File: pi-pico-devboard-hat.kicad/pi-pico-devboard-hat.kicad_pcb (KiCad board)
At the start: 2 copper layers, 65 x 56 mm, 28 parts, among them J1 Conn_01x24_Male, J2 I2C, J3 SDA_UP, J4 SCL_UP, J5 Conn_SPI, J6 Conn_Ext, J7 Conn_BTN, J8 Conn_LED, J9 Conn_02x03_Odd_Even, P1 Conn_02x20_Odd_Even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

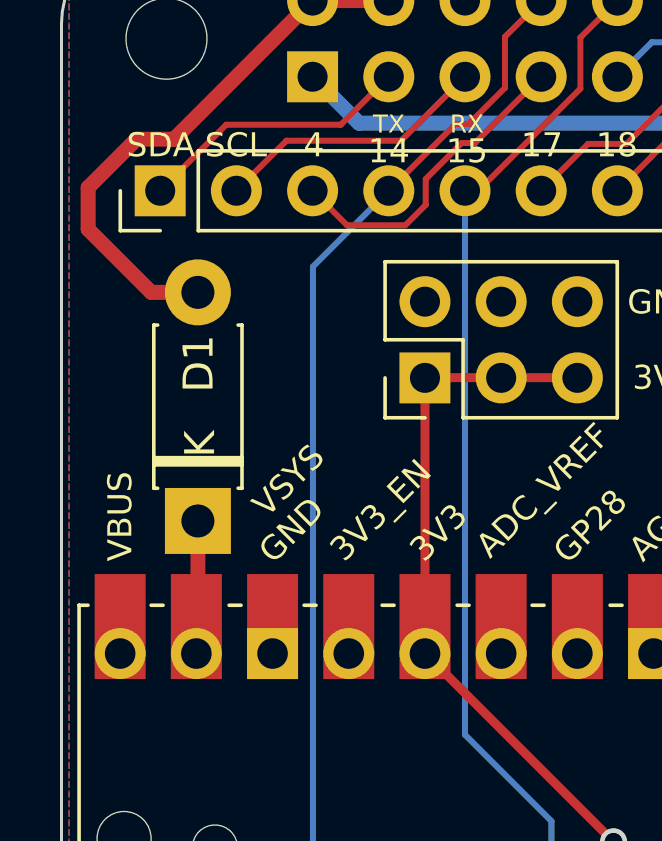
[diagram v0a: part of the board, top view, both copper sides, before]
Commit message: Rev 9: added master power-jumper
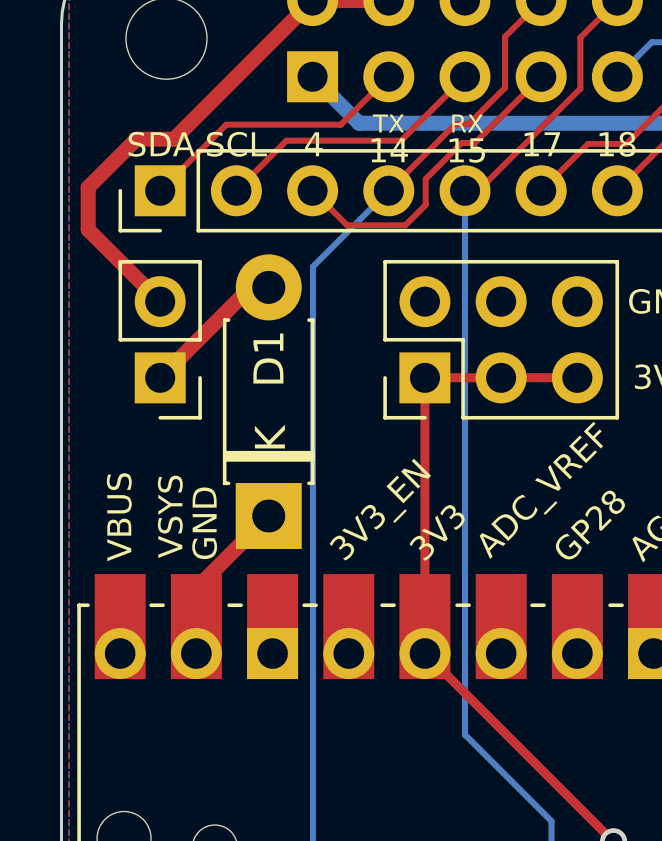
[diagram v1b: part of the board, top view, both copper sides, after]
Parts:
- added J10: Conn_Master_On, Connector_PinHeader_2.54mm:PinHeader_1x02_P2.54mm_Vertical, F.Cu at (203.3, 108.8)
- moved D1 2.37 mm to (206.9, 113.4)
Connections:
- D1 pad 2: +5V -> Net-(D1-Pad2)
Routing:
- net Net-(D1-Pad2): track 0.00 -> 5.47 mm
- net +5V: track 18.6 -> 17.4 mm
- net /VSYS: track 4.44 -> 5.66 mm
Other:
- board text added: "Rev: 9"
- board text removed: "Rev: 8"

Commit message: Rev 9.1: changed trace for 3V3
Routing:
- net /3V3: track 100.3 -> 117.6 mm, vias 1 -> 0
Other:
- net class 3V3: trace_width 0.3 -> 0.5
- board text added: "Rev: 9.1"
- board text removed: "Rev: 9"
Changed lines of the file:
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@@
   (net_class 3V3 ""
     (clearance 0.2)
-    (trace_width 0.3)
+    (trace_width 0.5)
     (via_dia 0.9)
     (via_drill 0.6)
@@
     (effects (font (size 0.8 0.8) (thickness 0.15)))
   )
-  (gr_text "Rev: 9" (at 203.9243 120.7138) (layer B.SilkS)
+  (gr_text "Rev: 9.1" (at 204.7371 120.6249) (layer B.SilkS)
     (effects (font (size 1 1) (thickness 0.15)) (justify mirror))
   )
@@
   (segment (start 204.4958 115.8243) (end 204.4958 117.996) (width 0.5) (layer F.Cu) (net 32))
   (segment (start 206.9088 113.4113) (end 204.4958 115.8243) (width 0.5) (layer F.Cu) (net 32))
-  (via (at 218.4023 124.2698) (size 0.9) (drill 0.6) (layers F.Cu B.Cu) (net 35))
-  (segment (start 212.1285 117.996) (end 218.4023 124.2698) (width 0.3) (layer F.Cu) (net 35))
   (segment (start 212.1158 117.996) (end 212.1285 117.996) (width 0.3) (layer F.Cu) (net 35))
-  (segment (start 254.5077 149.0602) (end 255.7149 147.853) (width 0.3) (layer B.Cu) (net 35))
-  (segment (start 254.1775 149.3904) (end 254.5077 149.0602) (width 0.3) (layer B.Cu) (net 35))
-  (segment (start 209.5758 147.662549) (end 209.5758 146.6726) (width 0.3) (layer B.Cu) (net 35))
-  (segment (start 211.31625 149.402999) (end 209.5758 147.662549) (width 0.3) (layer B.Cu) (net 35))
-  (segment (start 216.472001 149.402999) (end 211.31625 149.402999) (width 0.3) (layer B.Cu) (net 35))
-  (segment (start 218.4023 147.4727) (end 216.472001 149.402999) (width 0.3) (layer B.Cu) (net 35))
-  (segment (start 218.4023 124.2698) (end 218.4023 147.4727) (width 0.3) (layer B.Cu) (net 35))
-  (segment (start 224.0538 147.3457) (end 224.0538 146.6726) (width 0.3) (layer B.Cu) (net 35))
-  (segment (start 221.996501 149.402999) (end 224.0538 147.3457) (width 0.3) (layer B.Cu) (net 35))
-  (segment (start 219.558599 149.402999) (end 221.996501 149.402999) (width 0.3) (layer B.Cu) (net 35))
-  (segment (start 218.0086 147.853) (end 219.558599 149.402999) (width 0.3) (layer B.Cu) (net 35))
-  (segment (start 226.111099 149.402999) (end 224.0538 147.3457) (width 0.3) (layer B.Cu) (net 35))
-  (segment (start 230.885801 149.402999) (end 232.4358 147.853) (width 0.3) (layer B.Cu) (net 35))
-  (segment (start 226.111099 149.402999) (end 230.885801 149.402999) (width 0.3) (layer B.Cu) (net 35))
-  (segment (start 233.9732 149.3904) (end 254.1775 149.3904) (width 0.3) (layer B.Cu) (net 35))
-  (segment (start 232.4358 147.853) (end 233.9732 149.3904) (width 0.3) (layer B.Cu) (net 35))
-  (segment (start 212.1158 117.996) (end 212.1158 108.8012) (width 0.3) (layer F.Cu) (net 35))
-  (segment (start 212.1158 108.8012) (end 214.6558 108.8012) (width 0.3) (layer F.Cu) (net 35))
-  (segment (start 214.6558 108.8012) (end 217.1958 108.8012) (width 0.3) (layer F.Cu) (net 35))
+  (segment (start 207.3406 146.6726) (end 209.5758 146.6726) (width 0.5) (layer F.Cu) (net 35))
+  (segment (start 200.5461 139.8781) (end 207.3406 146.6726) (width 0.5) (layer F.Cu) (net 35))
+  (segment (start 200.5461 115.095698) (end 200.5461 139.8781) (width 0.5) (layer F.Cu) (net 35))
+  (segment (start 206.835398 108.8064) (end 200.5461 115.095698) (width 0.5) (layer F.Cu) (net 35))
+  (segment (start 212.1158 108.8064) (end 206.835398 108.8064) (width 0.5) (layer F.Cu) (net 35))
+  (segment (start 212.1158 117.996) (end 212.1158 108.8064) (width 0.5) (layer F.Cu) (net 35))
+  (segment (start 212.1158 108.8064) (end 214.6558 108.8064) (width 0.5) (layer F.Cu) (net 35))
+  (segment (start 214.6558 108.8064) (end 217.1958 108.8064) (width 0.5) (layer F.Cu) (net 35))
+  (segment (start 216.708599 149.153001) (end 218.0086 147.853) (width 0.5) (layer F.Cu) (net 35))
+  (segment (start 211.066252 149.153001) (end 216.708599 149.153001) (width 0.5) (layer F.Cu) (net 35))
+  (segment (start 209.5758 147.662549) (end 211.066252 149.153001) (width 0.5) (layer F.Cu) (net 35))
+  (segment (start 209.5758 146.6726) (end 209.5758 147.662549) (width 0.5) (layer F.Cu) (net 35))
+  (segment (start 221.573399 149.153001) (end 224.0538 146.6726) (width 0.5) (layer F.Cu) (net 35))
+  (segment (start 219.308601 149.153001) (end 221.573399 149.153001) (width 0.5) (layer F.Cu) (net 35))
+  (segment (start 218.0086 147.853) (end 219.308601 149.153001) (width 0.5) (layer F.Cu) (net 35))
+  (segment (start 231.135799 149.153001) (end 232.4358 147.853) (width 0.5) (layer F.Cu) (net 35))
+  (segment (start 226.534201 149.153001) (end 231.135799 149.153001) (width 0.5) (layer F.Cu) (net 35))
+  (segment (start 224.0538 146.6726) (end 226.534201 149.153001) (width 0.5) (layer F.Cu) (net 35))
+  (segment (start 254.414899 149.153001) (end 255.7149 147.853) (width 0.5) (layer F.Cu) (net 35))
+  (segment (start 233.735801 149.153001) (end 254.414899 149.153001) (width 0.5) (layer F.Cu) (net 35))
+  (segment (start 232.4358 147.853) (end 233.735801 149.153001) (width 0.5) (layer F.Cu) (net 35))
   (segment (start 227.3558 112.8374) (end 227.3304 112.812) (width 0.2) (layer F.Cu) (net 38))
   (segment (start 227.3558 117.996) (end 227.3558 112.8374) (width 0.2) (layer F.Cu) (net 38))

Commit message: Rev 10: reorg of I2C-pullup connector
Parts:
- removed J4: SCL_UP, Connector_PinHeader_2.54mm:PinHeader_1x02_P2.54mm_Vertical
- J3: value SDA_UP -> Conn_PU; footprint Connector_PinHeader_2.54mm:PinHeader_1x02_P2.54mm_Vertical -> Connector_PinHeader_2.54mm:PinHeader_1x04_P2.54mm_Vertical
- moved J3 8.01 mm to (212.9, 141.6), turned to 90 degrees
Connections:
- J3 pad 1: /SCL_GP3 -> Net-(J3-Pad1)
- J3 pad 2: Net-(J3-Pad2) -> /SDA_GP2
- R1 pad 2: Net-(J3-Pad2) -> Net-(J3-Pad4)
- R2 pad 2: Net-(J4-Pad2) -> Net-(J3-Pad1)
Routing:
- net Net-(J3-Pad4): track 0.00 -> 3.53 mm
- net Net-(J3-Pad2): track 3.53 -> 0.00 mm
- net Net-(J4-Pad2): track 3.35 -> 0.00 mm
- net Net-(J3-Pad1): track 0.00 -> 3.35 mm
- net /SCL_GP3: track 19.4 -> 16.5 mm
- net /SDA_GP2: track 13.8 -> 16.5 mm
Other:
- board text added: "GP2 SDA"
- board text added: "GP3 SCL"
- board text added: "Rev: 10"
- board text removed: "+"
- board text removed: "-"
- board text removed: "Rev: 9.1"
- board text removed: "SCL/GP3"
- board text removed: "SDA/GP2"

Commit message: Rev 11: connect Pi-pins GPIO16/GPIO26 to pin-connector (remove GPIO24/GPIO25 used for SWD)
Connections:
- J1 pad 11: /GPIO24(GEN5) -> /GPIO10(SPI0_MOSI)
- J1 pad 12: /GPIO25(GEN6) -> /GPIO9(SPI0_MISO)
- J1 pad 13: /GPIO10(SPI0_MOSI) -> /GPIO11(SPI0_SCK)
- J1 pad 14: /GPIO9(SPI0_MISO) -> /GPIO8(SPI0_CE_0)
- J1 pad 15: /GPIO11(SPI0_SCK) -> /GPIO7(SPI0_CE_1)
- J1 pad 16: /GPIO8(SPI0_CE_0) -> /GPIO5
- J1 pad 17: /GPIO7(SPI0_CE_1) -> /GPIO6
- J1 pad 18: /GPIO5 -> /GPIO12(PWM0)
- J1 pad 19: /GPIO6 -> /GPIO13(PWM1)
- J1 pad 20: /GPIO12(PWM0) -> /GPIO19(SPI1_MISO)
- J1 pad 21: /GPIO13(PWM1) -> /GPIO16
- J1 pad 22: /GPIO19(SPI1_MISO) -> /GPIO26
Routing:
- net /GPIO16: track 0.00 -> 7.39 mm
- net /GPIO26: track 0.00 -> 4.85 mm
- net /GPIO13(PWM1): track 6.65 -> 3.80 mm
- net /GPIO19(SPI1_MISO): track 6.65 -> 3.80 mm
- net /GPIO8(SPI0_CE_0): track 9.44 -> 7.40 mm
- net /GPIO7(SPI0_CE_1): track 8.70 -> 7.29 mm
- net /GPIO12(PWM0): track 8.83 -> 7.49 mm
- net /GPIO24(GEN5): track 39.7 -> 40.9 mm
- net /GPIO25(GEN6): track 42.0 -> 40.9 mm
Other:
- board text added: "Rev: 11"
- board text removed: "Rev: 10"

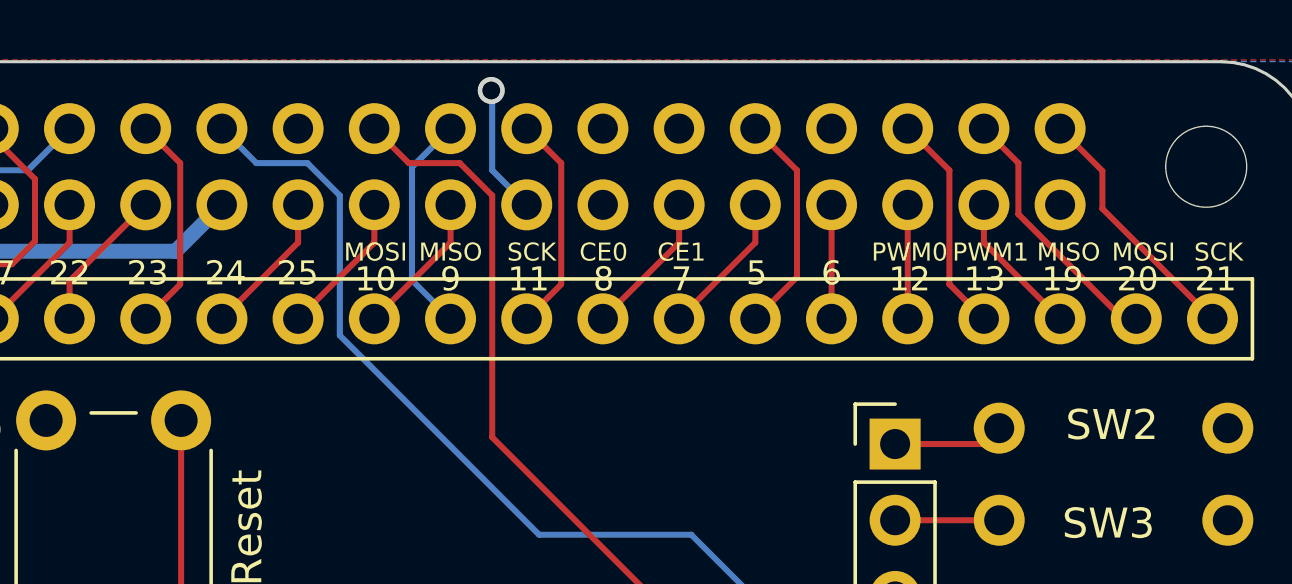
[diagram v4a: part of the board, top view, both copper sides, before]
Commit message: fixed labels of Pi-pin-connector
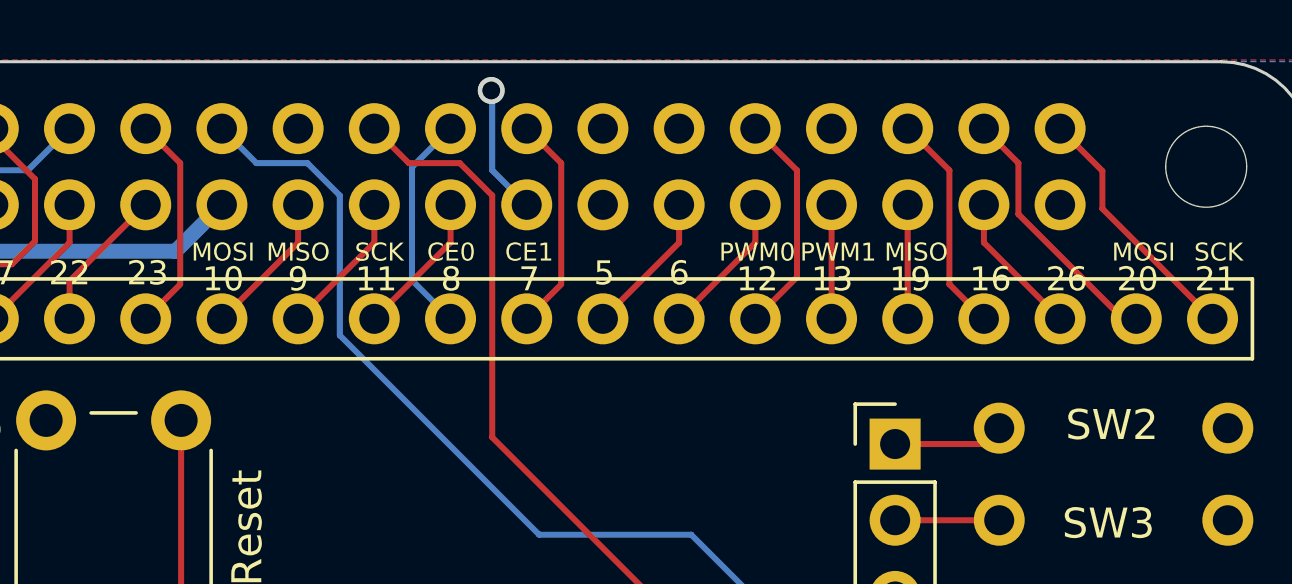
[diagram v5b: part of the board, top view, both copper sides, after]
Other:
- board text added: "16"
- board text added: "26"
- board text removed: "24"
- board text removed: "25"

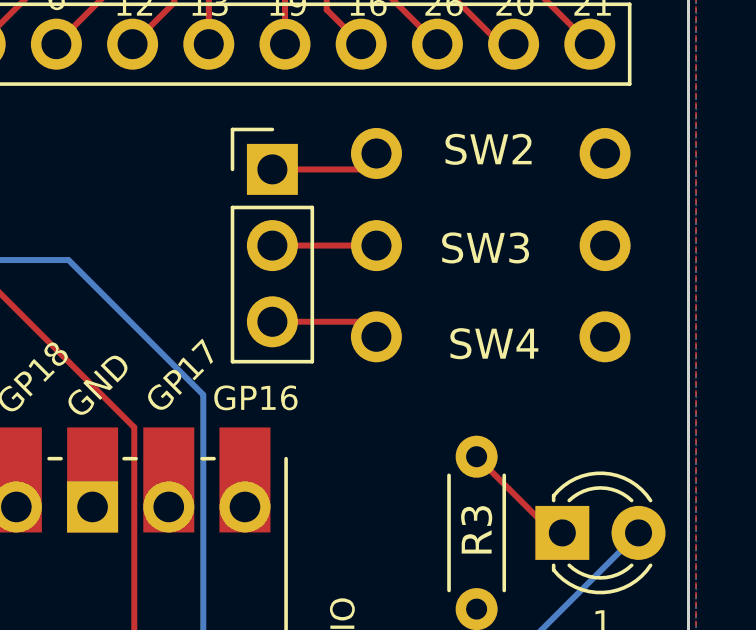
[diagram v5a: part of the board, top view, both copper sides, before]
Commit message: fixed footprint and position of SW2-SW4
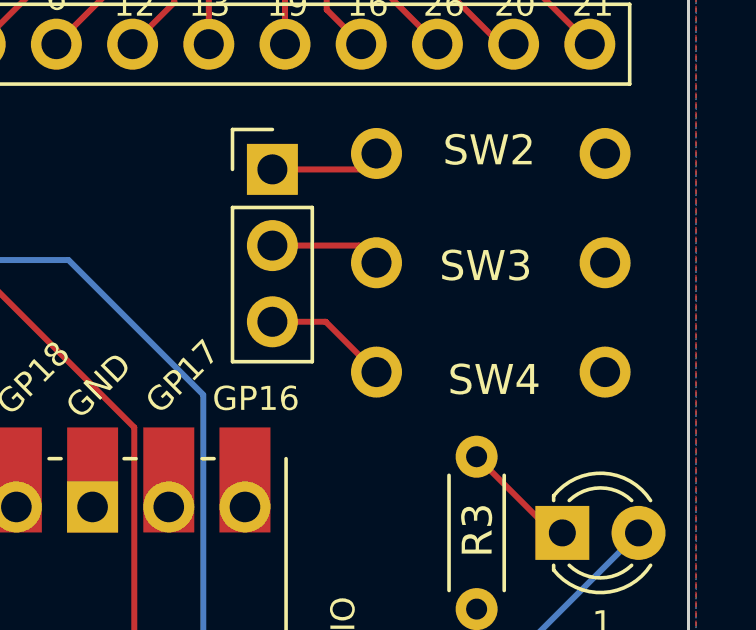
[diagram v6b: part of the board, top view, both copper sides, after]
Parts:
- moved SW4 1.18 mm to (254.6, 113.5)
- moved SW3 0.57 mm to (254.6, 109.9)
